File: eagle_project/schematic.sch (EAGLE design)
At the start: 216 parts, among them IC2 AZ34063U, IC3 AZ34063U, IC4 LM358A, IC5 PIC24FJ64GU202-I_SS, IC6 LM358A, IC7 AZ34063U, J1 USB-B, Q1 16MHz, U1 OP07CD, U11 OP07CD, U12 OP07CD, U14 MCP4912-E/SL, U2 OP07CD, U3 OP07CD, U4 MCP1501T-40E/CHY, U5 OP07CD, U6 OP07CD, U7 OP07CD, U8 OP07CD, X1 MKDSN1,5/4-5,08, X2 MKDSN1,5/4-5,08, X3 MKDSN1,5/4-5,08, X4 MKDSN1,5/2-5,08, X5 MKDSN1,5/2-5,08, X6 MKDSN1,5/2-5,08, X7 MKDSN1,5/2-5,08, X8 MKDSN1,5/3-5,08

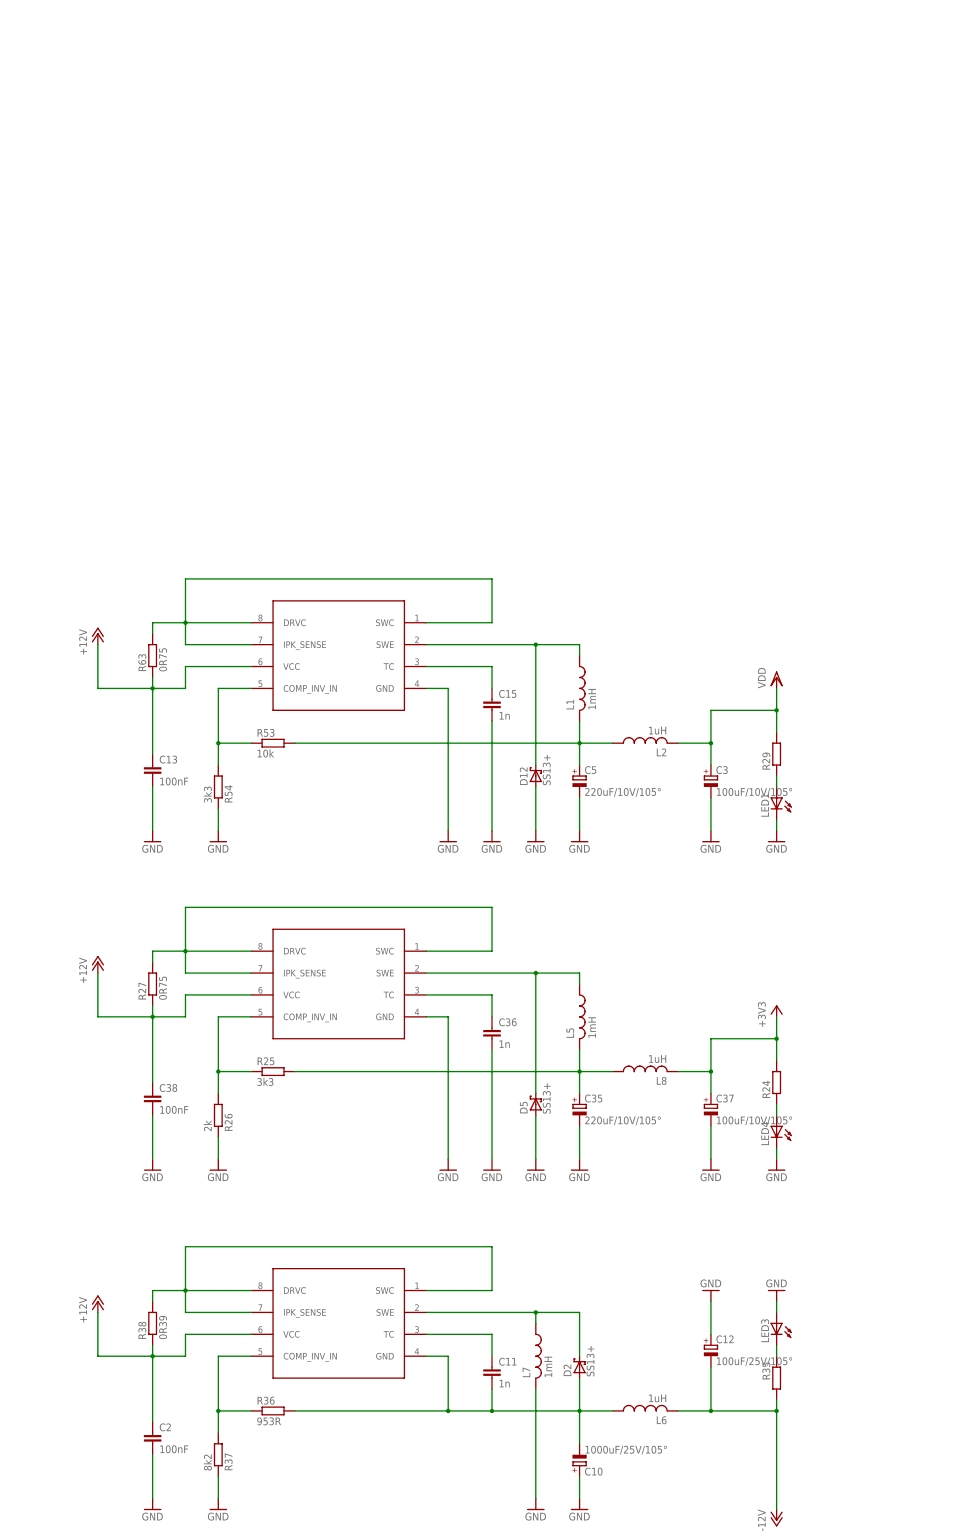
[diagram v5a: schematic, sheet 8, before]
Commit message: Reverted DI. Added linear +-12V PSU with transformer
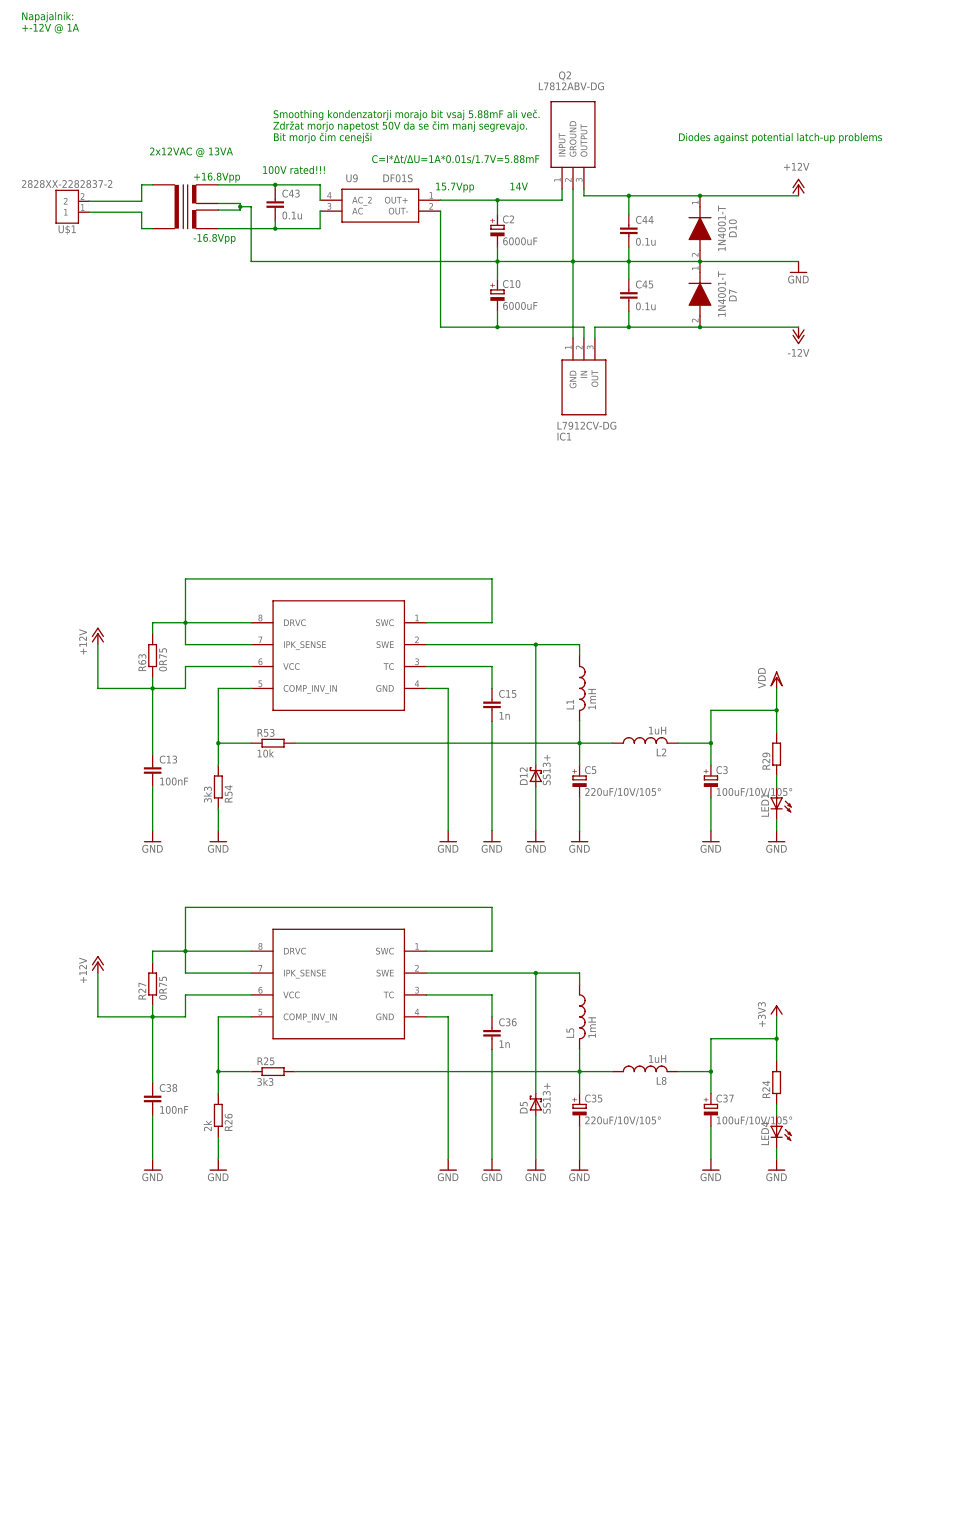
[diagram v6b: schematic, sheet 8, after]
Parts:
- removed C11: 1n, rcl:C-EUC0805
- removed C12: 100uF/25V/105°, rcl:CPOL-EUE2-5
- removed D2: SS13+, diode:SCHOTTKY-DIODESMC
- removed IC2: AZ34063U, IMPORTED_ELEMENTS:AZ34063U
- removed L6: 1uH, IMPORTED:INDUCTOR
- removed L7: 1mH, SamacSys_Parts:12LRS105C
- removed LED10, LED9: (no value), led:LEDCHIPLED_0805
- removed LED3: (no value), led:LED3MM
- removed R104, R105: 1k, rcl:R-EU_R0805
- removed R33, R56: 750, rcl:R-EU_0309/12
- removed R35: (no value), rcl:R-EU_R0805
- removed R36: 953R, rcl:R-EU_R0805
- removed R37: 8k2, rcl:R-EU_R0805
- removed R38: 0R39, rcl:R-EU_R0805
- removed R55: 600, rcl:R-EU_0309/12
- removed S3: TL36PO, switch:TL36PO
- added C41, C42, C9: 100n, rcl:C-EUC0805
- added C43, C44, C45: 0.1u, rcl:C-EUC0805
- added D10: 1N4001-T, SamacSys_Parts:1N4001-T
- added D8: 1N4148, diode:1N4148
- added IC1: L7912CV-DG, SamacSys_Parts:L7912CV-DG
- added Q2: L7812ABV-DG, SamacSys_Parts:L7812ABV-DG
- added TR1: TRANSFORMER-PCB-2X12, DelavnicaCustomComponents:TRANSFORMER-PCB-2X12
- added U$1: 2828XX-2282837-2, Connector:2828XX-2282837-2
- added U9: DF01S, SamacSys_Parts:DF01S
- C10: value 1000uF/25V/105° -> 6000uF; device rcl:CPOL-EUE5-13 -> rcl:CPOL-EUE10-22.5
- C2: value 100nF -> 6000uF; device rcl:C-EUC0805 -> rcl:CPOL-EUE10-22.5
- D1, D6: value BZX55 -> 1N4148; device diode:BZX55 -> diode:1N4148
- D7: value BZX55 -> 1N4001-T; device diode:BZX55 -> SamacSys_Parts:1N4001-T
- R21: value 750 -> 1k; device rcl:R-EU_0309/12 -> rcl:R-EU_R2512
- R31, R32: value 600 -> 1k; device rcl:R-EU_0309/12 -> rcl:R-EU_R2512
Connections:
- removed net +5V2: C10.-, C11.2, D2.A, IC2.GND, L6.1, R36.2
- removed net N$120: LED10.A, R105.1
- removed net N$19: LED3.C, R35.1
- removed net N$31: IC2.COMP_INV_IN, R36.1, R37.2
- removed net N$33: IC2.DRVC, IC2.IPK_SENSE, IC2.SWC, R38.2
- removed net N$34: C11.1, IC2.TC
- removed net N$42: D2.C, IC2.SWE, L7.1
- removed net PROG: R105.2, S3.O
- removed net RUN: R104.2, S3.S
- new net N$121: C43.1, TR1.S11, U9.AC_2
- new net N$122: C43.2, TR1.S22, U9.AC
- new net N$123: D8.C, X5-2.KL
- new net N$124: C2.+, Q2.INPUT, U9.OUT+
- new net N$125: C10.-, IC1.IN, U9.OUT-
- net +12V: now also C44.1, D10.K, Q2.OUTPUT; no longer C2.1, IC2.VCC, R38.1
- net -12V: now also C45.2, D7.A, IC1.OUT; no longer C12.-, L6.2, R35.2
- net GND: now also C2.-, C44.2, C45.1, D10.A, D7.K, IC1.GND, Q2.GROUND, TR1.S12, TR1.S21; no longer C12.+, C2.2, L7.2, LED10.C, LED3.A, LED9.C, R37.1
- net N$115: now also TR1.P2, U$1.1; no longer OK4.A, R21.2
- net N$119: now also TR1.P1, U$1.2; no longer LED9.A, R104.1
- net N$13: now also R21.1; no longer R32.1
- net N$17: now also C41.1, OK1.A, R21.2; no longer D1.A, OK1.C, X6-2.KL
- net N$21: now also C41.2, D1.A, OK1.C; no longer D1.C, R32.2, R33.1
- net N$29: now also D1.C, X6-2.KL; no longer OK1.A, R33.2
- net N$39: now also C9.2, D8.A; no longer D6.A, X5-2.KL
- net N$54: now also R32.1; no longer R55.1
- net N$57: now also C42.1, OK2.A, R32.2; no longer D7.A, OK2.C, X7-2.KL
- net N$61: now also C42.2, D6.A, OK2.C; no longer D7.C, R55.2, R56.1
- net N$67: now also D6.C, X7-2.KL; no longer OK2.A, R56.2
- net N$84: now also C9.1, OK4.A; no longer D6.C, R21.1
- net VCC: no longer S3.P
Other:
- note added: "+16.8Vpp"
- note added: "-16.8Vpp"
- note added: "100V rated!!!"
- note added: "14V"
- note added: "15.7Vpp"
- note added: "2x12VAC @ 13VA"
- note added: "5 - 48 V"
- note added: "C=I*Δt/ΔU=1A*0.01s/1.7V=5.88mF"
- note added: "Diodes against potential latch-up problems"
- note added: "Napajalnik: +-12V @ 1A"
- note added: "SFH615A-3X: Vf=1.2V @ 10mA"
- note added: "Smoothing kondenzatorji morajo bit vsaj 5.88mF ali več. Zdržat morjo napetost 50V da se čim manj segrevajo. Bit morjo čim cenejši"
- note removed: "HCPL-817-300E: Vf=1.2V @ 20mA"
- note removed: "R=(Vin-Vz)/(Iz+IL)=(30V-15V)/(5mA+20mA)=600Ω P=I^2*R=0.375W"
- note removed: "R=U/I=15V/20mA=750Ω P=I^2*R=0.3W"
- note removed: "Vz=15V"
- moved on the sheet: C10, JP2, R21, R31, R32, X5-1, X5-2, X6-1, X6-2, X7-1, X7-2
